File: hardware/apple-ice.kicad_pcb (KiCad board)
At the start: 2 copper layers, 100 x 77.7 mm, 80 parts, among them J1 TO_SP_DRIVE, J2 USB_B_Micro, J3 SPI_FLASH_PROG, P1 A2Bus-apple2, SW1 SW_Push, SW2 SW_Push, SW3 SW_Push, U1 SN74LVC8T245PW, U10 W25Q16JVSS, U2 SN74LVC8T245PW, U3 SN74LVC8T245PW, U4 SN74LVC8T245PW, U5 SN74LVC8T245PW, U6 ICE40HX1K-TQ144, U7 SN74LVC8T245PW, U8 MCP1703A-3302_SOT223, U9 MCP1703A-1202_SOT223, X1 ECS-2520MV-xxx-xx

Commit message: More routing, 80% finished
Signed-off-by: Rangel Ivanov <rangelivanov88@gmail.com>
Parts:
- moved C25 12.8 mm to (102.2, 33.9), turned to 180 degrees
- moved SW1 6.17 mm to (187.8, 62.8)
- moved R21 5.56 mm to (160.1, 65.5), turned to 90 degrees
- moved R22 5.43 mm to (170.4, 58.5), turned to 270 degrees
- moved U10 4.72 mm to (164.1, 60.2)
- moved C26 4.60 mm to (167.8, 55.3)
- moved R13 4.05 mm to (158.5, 65.5), turned to 90 degrees
- moved J3 3.61 mm to (178.5, 69.4), turned to 180 degrees
- moved R14 2.95 mm to (159.6, 56.5)
- moved R20 2.24 mm to (170.3, 66.2)
- moved D3 2.22 mm to (166.9, 66.2)
- moved R19 2.22 mm to (163.6, 66.2)
- moved C13 2.00 mm to (162.1, 73.6)
- moved C16 2.00 mm to (162.1, 72.1)
- moved R11 1.53 mm to (101.6, 38.5)
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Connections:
- J1 pad 9: -12V -> Net-(J1-Pad9)
- P1 pad 33: -12V -> Net-(P1-Pad33)
- U10 pad 2: /iC40_SDO -> /iC40_SDI
- U10 pad 5: /iC40_SDI -> /iC40_SDO
- U6 pad 101: Net-(U6-Pad101) -> /BTN1
- U6 pad 102: Net-(U6-Pad102) -> /BTN2
- U6 pad 105: Net-(U6-Pad105) -> /USB_N
- U6 pad 106: Net-(U6-Pad106) -> /USB_P
- U6 pad 107: Net-(U6-Pad107) -> /USB_PU
- U6 pad 63: Net-(U6-Pad63) -> /~FLASH_WP(~IO3)
- U6 pad 64: Net-(U6-Pad64) -> /~FLASH_HOLD(~IO4)
- U6 pad 78: /~FLASH_WP(~IO3) -> Net-(U6-Pad78)
- U6 pad 79: /~FLASH_HOLD(~IO4) -> Net-(U6-Pad79)
- U6 pad 80: /BTN1 -> Net-(U6-Pad80)
- U6 pad 81: /BTN2 -> Net-(U6-Pad81)
- U6 pad 90: /USB_P -> Net-(U6-Pad90)
- U6 pad 91: /USB_N -> Net-(U6-Pad91)
- U6 pad 95: /USB_PU -> Net-(U6-Pad95)
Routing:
- net +3.3V: track 153.7 -> 236.1 mm
- net +12V: track 0.00 -> 77.0 mm
- net /USB_N: track 0.00 -> 45.4 mm
- net /USB_PU: track 0.00 -> 43.7 mm
- net /USB_P: track 0.00 -> 43.3 mm
- net /~iCE40_CRESET: track 0.00 -> 43.1 mm
- net /BTN1: track 0.00 -> 38.3 mm
- net /~iCE40_CS: track 0.00 -> 37.6 mm
- net /BTN2: track 0.00 -> 32.9 mm
- net /iCE40_SCK: track 0.00 -> 30.4 mm
- net /iC40_SDI: track 0.00 -> 29.7 mm
- net /iCE40_CDONE: track 0.00 -> 28.0 mm
- net /iC40_SDO: track 0.00 -> 24.0 mm
- net +1V2: track 114.9 -> 91.5 mm, vias 17 -> 14
- net /~FLASH_HOLD(~IO4): track 0.00 -> 20.0 mm, vias 0 -> 2
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- added copper zone on B.Cu, net GND

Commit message: Finish routing
Signed-off-by: Rangel Ivanov <rangelivanov88@gmail.com>
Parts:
- added C32: 1u, apple-ice:C_0603_1608Metric_Pad1.08x0.95mm_HandSolder, B.Cu at (154.6, 73.4)
- added C37: 100n, apple-ice:C_0603_1608Metric_Pad1.08x0.95mm_HandSolder, B.Cu at (155.9, 69.9)
- turned C25 to 0 degrees
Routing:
- net GND: track 0.66 -> 96.4 mm, vias 0 -> 166
- net +5V: track 161.2 -> 199.7 mm, vias 3 -> 4
- net Net-(P1-Pad24): track 0.00 -> 8.94 mm, vias 0 -> 1
- net Net-(P1-Pad23): track 0.00 -> 8.92 mm, vias 0 -> 1
- net +3.3V: track 236.1 -> 243.2 mm
- net +1V2: track 91.5 -> 98.4 mm, vias 14 -> 16
- net /RW: track 45.2 -> 46.0 mm
- added copper zone on F.Cu, net GND

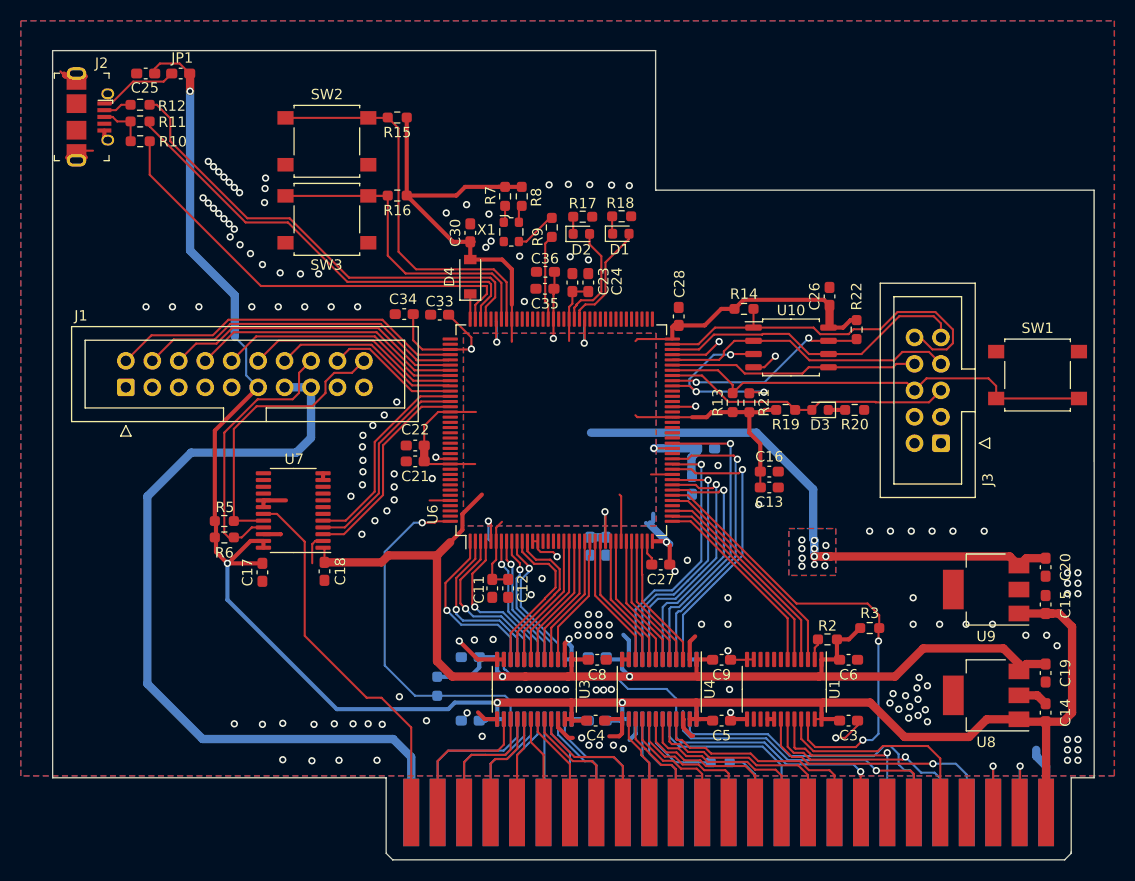
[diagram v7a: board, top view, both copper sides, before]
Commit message: Remove some vias
Signed-off-by: Rangel Ivanov <rangelivanov88@gmail.com>
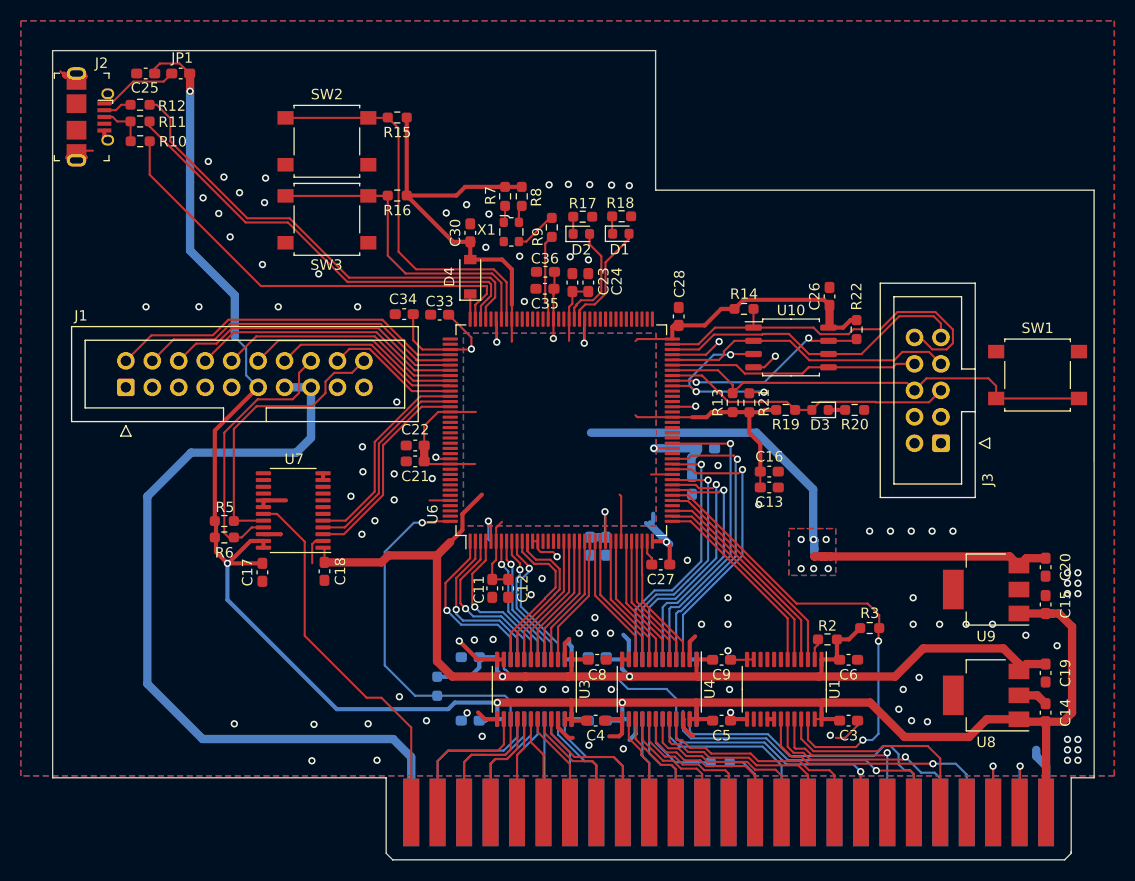
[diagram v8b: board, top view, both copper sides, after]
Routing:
- net GND: vias 166 -> 107
- net +1V2: vias 16 -> 11
